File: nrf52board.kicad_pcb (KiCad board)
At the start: 2 copper layers, 27.9 x 59.7 mm, 47 parts, among them J1 Conn_01x04, J2 USB_B_Micro, J3 Battery, Q1 Q_PMOS_DSG, SW1 SW_Push, SW2 SW_Push, U1 nrf52board, U2 E73-2G4M04S, U3 MCP73831-2-OT, U4 LP2985-3.3, U5 RFM95W-868S2, U6 CP2102-GM

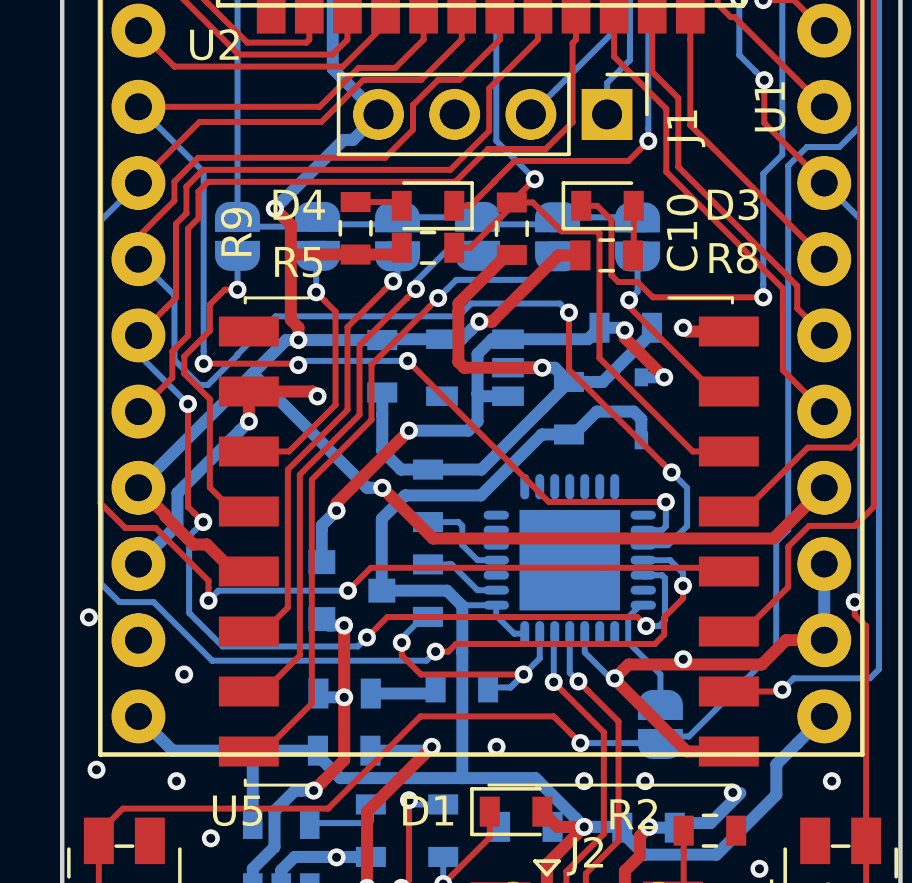
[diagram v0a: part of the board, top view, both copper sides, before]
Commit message: Update Q1 on PCB
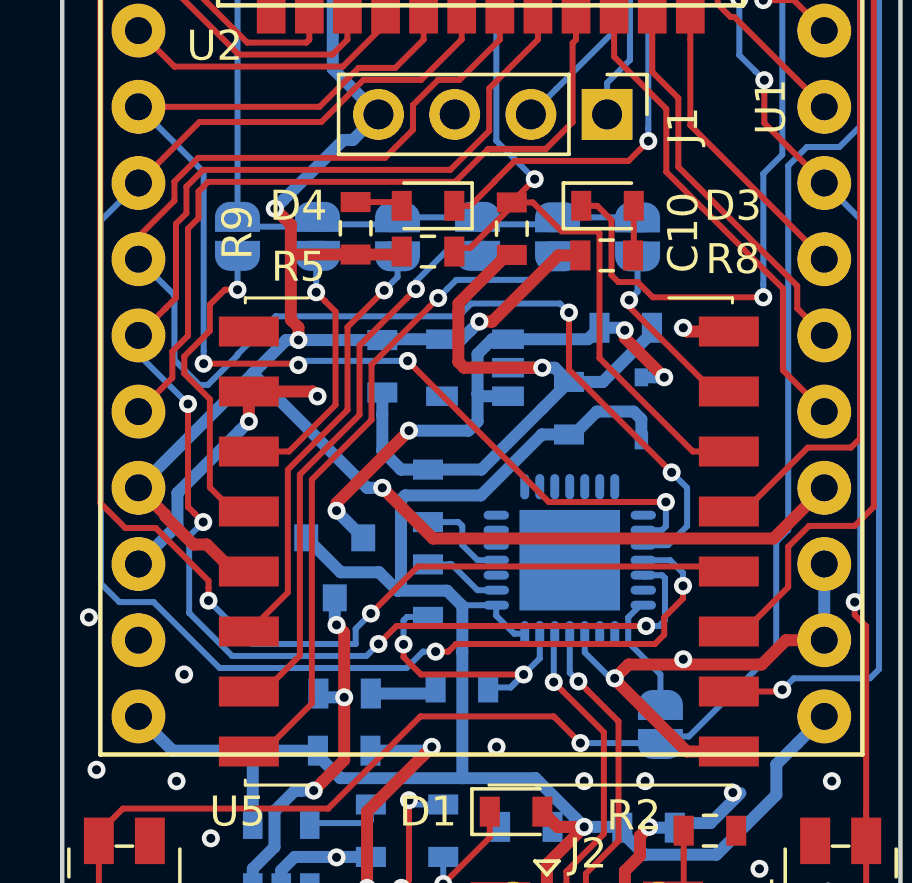
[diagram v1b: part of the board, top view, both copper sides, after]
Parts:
- Q1: value Q_PMOS_DSG -> PMV65XP
- moved Q1 0.95 mm to (66.1, 95.4), turned to 270 degrees
- moved R5 0.13 mm to (69.2, 84.8)
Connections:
- Q1 pad 1: +BATT -> +5V
- Q1 pad 3: +5V -> +BATT
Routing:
- net +5V: track 60.6 -> 63.6 mm
- net P0.25: track 73.3 -> 74.8 mm
- net Net-(C8-Pad2): track 19.7 -> 19.1 mm

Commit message: Fix BOM
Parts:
- D1, D3, D4: value LED -> LC191yct
- D2: value D_Schottky -> NSR1020MW2
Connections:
- J2 pad 4: Net-(J2-Pad4) -> (no net)
- U4 pad 4: Net-(U4-Pad4) -> (no net)
- U5 pad 9: Net-(U5-Pad9) -> (no net)
- U6 pad 1: Net-(U6-Pad1) -> (no net)
- U6 pad 10: Net-(U6-Pad10) -> (no net)
- U6 pad 12: Net-(U6-Pad12) -> (no net)
- U6 pad 13: Net-(U6-Pad13) -> (no net)
- U6 pad 14: Net-(U6-Pad14) -> (no net)
- U6 pad 15: Net-(U6-Pad15) -> (no net)
- U6 pad 16: Net-(U6-Pad16) -> (no net)
- U6 pad 17: Net-(U6-Pad17) -> (no net)
- U6 pad 18: Net-(U6-Pad18) -> (no net)
- U6 pad 19: Net-(U6-Pad19) -> (no net)
- U6 pad 2: Net-(U6-Pad2) -> (no net)
- U6 pad 20: Net-(U6-Pad20) -> (no net)
- U6 pad 21: Net-(U6-Pad21) -> (no net)
- U6 pad 22: Net-(U6-Pad22) -> (no net)
- U6 pad 27: Net-(U6-Pad27) -> (no net)
